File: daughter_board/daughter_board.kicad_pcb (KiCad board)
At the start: 2 copper layers, 54.1 x 62.5 mm, 30 parts, among them J1 Conn_01x05_Female, J3 Conn_01x06_Male, J4 Conn_01x06_Male, J5 Conn_01x02_Male, J6 Conn_01x02_Male, J7 Conn_01x06_Male, J8 Conn_01x06_Male, U1 ATmega32U4-A, U2 DRV8833PW, U3 DRV8833PW, U4 DRV8833PW, Y1 Crystal

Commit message: im so tired
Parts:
- removed C10: 0.1uF, Capacitor_SMD:C_0805_2012Metric
- removed C12: 2.2uF, Capacitor_SMD:C_0805_2012Metric
- removed C13: 10uF, Capacitor_SMD:C_0805_2012Metric
- removed J5, J6: Conn_01x02_Male, Connector_PinHeader_1.27mm:PinHeader_1x02_P1.27mm_Vertical
- removed U3: DRV8833PW, Package_SO:TSSOP-16_4.4x5mm_P0.65mm
- added SW1: SW_Push, Button_Switch_SMD:SW_SPST_EVPBF, F.Cu at (76.3, 100.2)
- C1, C11, C14, C15, C2, C3, C4, C5, C6, C7, C8, C9: footprint Capacitor_SMD:C_0805_2012Metric -> Capacitor_SMD:C_0402_1005Metric
- Y1: footprint Crystal:Crystal_SMD_SeikoEpson_FA238-4Pin_3.2x2.5mm -> Crystal:TXC_A308000003
- moved J8 61.0 mm to (66.1, 104.3)
- moved C11 54.2 mm to (69.7, 99.1)
- moved J4 53.1 mm to (58.7, 104.1), turned to -90 degrees
- moved C3 49.7 mm to (51.7, 100.8), turned to 150 degrees
- moved C8 42.2 mm to (49.0, 92.8)
- moved C14 39.6 mm to (69.2, 97.6), turned to 90 degrees
- moved R2 39.1 mm to (48.7, 101.4)
- moved C9 38.0 mm to (46.9, 86.0)
- moved C6 37.7 mm to (49.7, 86.8), turned to -120 degrees
- moved R1 37.2 mm to (48.7, 100.2)
- moved C5 36.6 mm to (50.8, 87.5), turned to -120 degrees
- moved U4 36.6 mm to (65.7, 98.6), turned to 90 degrees
- moved C1 35.0 mm to (47.6, 92.5), turned to 150 degrees
- moved U2 34.8 mm to (46.0, 89.4), turned to 0 degrees
- moved J3 33.7 mm to (40.8, 94.0)
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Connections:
- C15 pad 1: Net-(C15-Pad1) -> MOTOR_SUPPLY
- C9 pad 1: Net-(C9-Pad1) -> MOTOR_SUPPLY
- J8 pad 3: /D_ENC_1 -> Net-(J8-Pad3)
- J8 pad 6: Net-(J8-Pad6) -> /D_ENC_1
- U1 pad 13: unconnected-(U1-Pad13) -> RST
- U1 pad 20: MOTOR_B2_IN -> MOTOR_B1_IN
- U1 pad 21: MOTOR_B1_IN -> MOTOR_B2_IN
- U1 pad 28: /C_ENC_1 -> /C_ENC_2
- U1 pad 29: /C_ENC_2 -> /C_ENC_1
- U1 pad 31: MOTOR_A2_IN -> MOTOR_A1_IN
- U1 pad 32: MOTOR_A1_IN -> MOTOR_A2_IN
- U2 pad 12: Net-(C9-Pad1) -> MOTOR_SUPPLY
- U4 pad 12: Net-(C15-Pad1) -> MOTOR_SUPPLY
- U4 pad 7: Net-(J8-Pad6) -> Net-(J8-Pad3)
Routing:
- net Net-(J7-Pad2): track 0.00 -> 36.4 mm, vias 0 -> 2
- net Net-(J7-Pad1): track 0.00 -> 35.9 mm, vias 0 -> 2
- net +3V3: track 0.00 -> 34.5 mm, vias 0 -> 4
- net /D_ENC_1: track 0.00 -> 30.7 mm, vias 0 -> 2
- net GND: track 0.00 -> 30.1 mm, vias 0 -> 5
- net RST: track 0.00 -> 28.3 mm, vias 0 -> 2
- net /B_ENC_2: track 0.00 -> 28.2 mm, vias 0 -> 2
- net Net-(J4-Pad1): track 0.00 -> 24.5 mm
- net /B_ENC_1: track 0.00 -> 24.2 mm, vias 0 -> 2
- net Net-(J4-Pad2): track 0.00 -> 22.6 mm
- net /C_ENC_2: track 0.00 -> 18.8 mm
- net /C_ENC_1: track 0.00 -> 16.1 mm
- net MOTOR_A2_IN: track 0.00 -> 15.3 mm, vias 0 -> 1
- net MOTOR_B2_IN: track 0.00 -> 14.1 mm, vias 0 -> 1
- net MOTOR_C1_IN: track 0.00 -> 14.0 mm, vias 0 -> 1
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- added copper zone on In1.Cu, net +3V3
- added copper zone on B.Cu, net GND
- added copper zone on F.Cu, net GND
- added copper zone on In1.Cu, net GND
- added copper zone on In2.Cu, net GND
- added copper zone on In2.Cu, net MOTOR_SUPPLY
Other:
- board size 54.1 x 62.5 mm -> 54.1 x 31.2 mm
- copper layers 2 -> 4
- board text added: "3V3"
- board text added: "ENC"
- board text added: "GND"
- board text added: "M_Out"
- board text added: "RST"
- board text added: "SCL"
- board text added: "SDA"
- board text added: "VM"

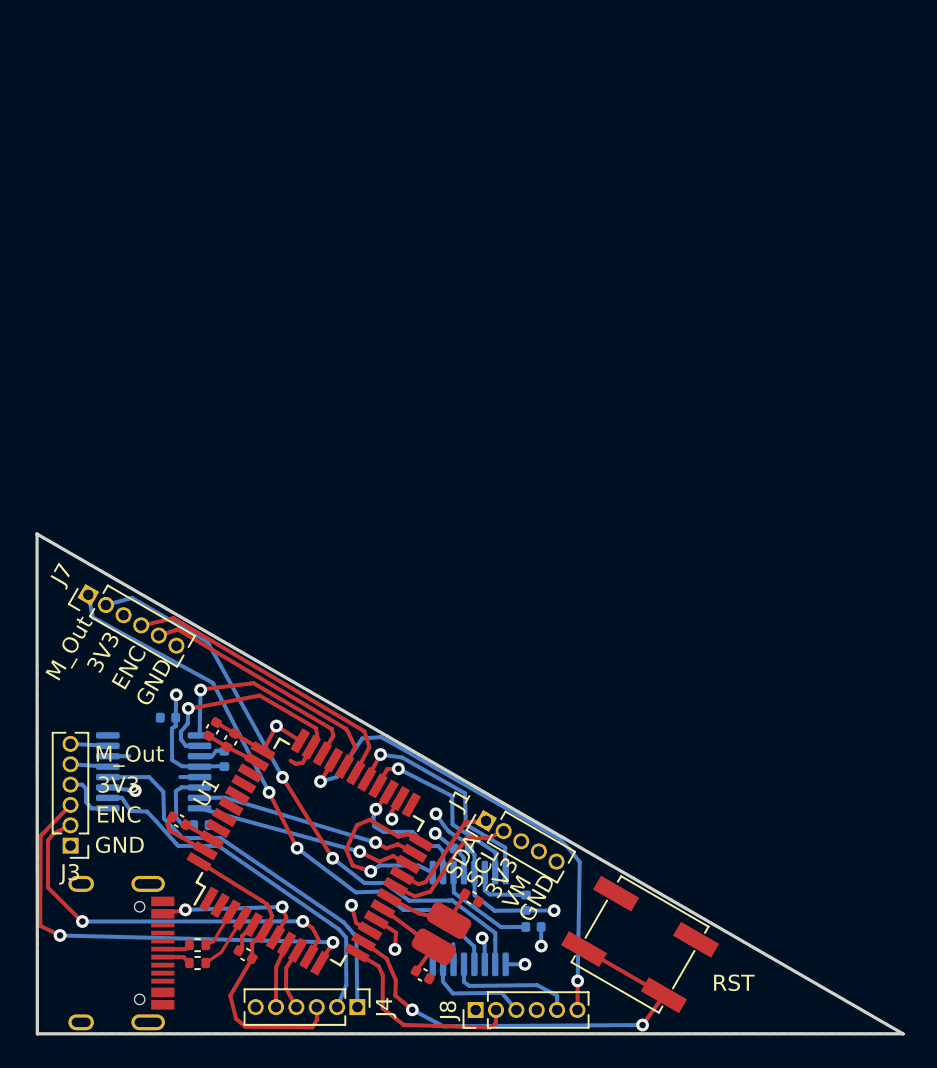
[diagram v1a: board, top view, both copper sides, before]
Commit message: Added daughter board
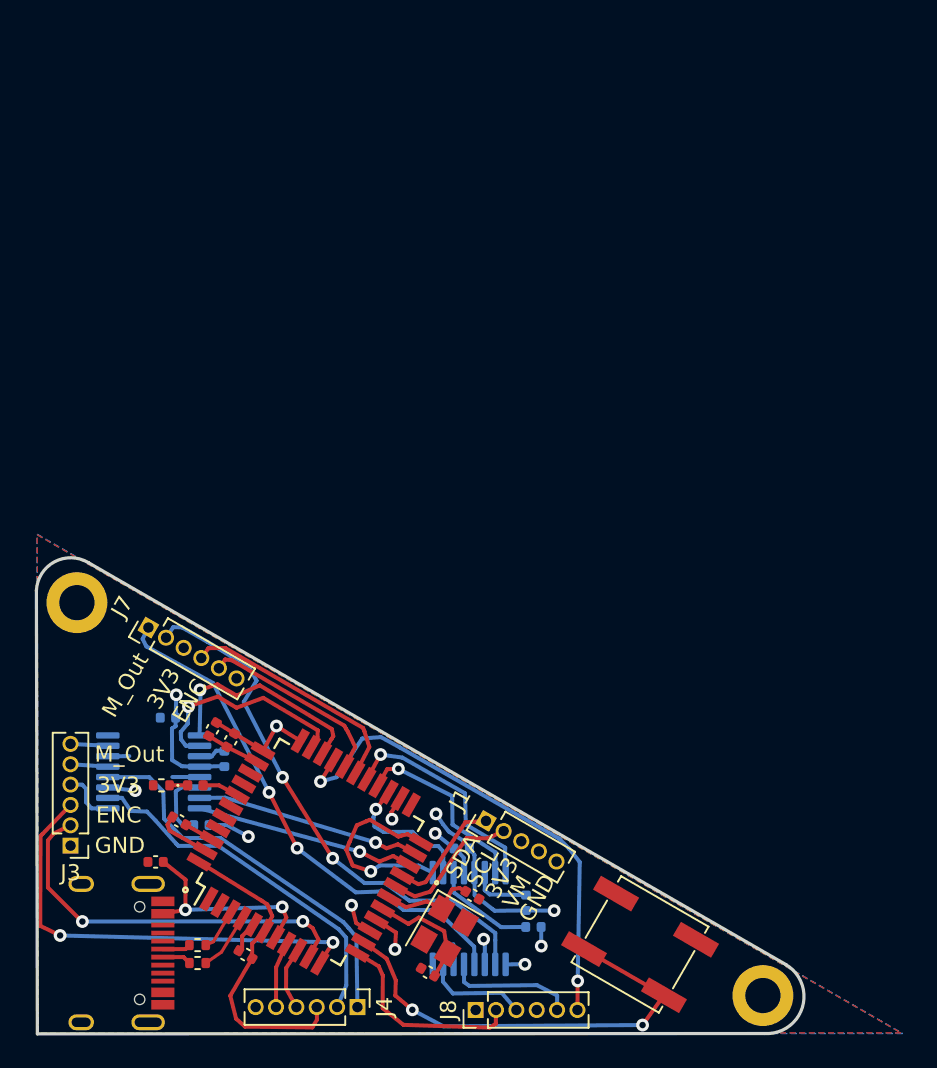
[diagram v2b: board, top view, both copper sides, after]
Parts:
- added C10: 0.1uF, Capacitor_SMD:C_0402_1005Metric, F.Cu at (46.1, 95.0)
- added D1: LED, LED_SMD:LED_0402_1005Metric, F.Cu at (48.6, 90.3)
- added H1: MountingHole_Pad, MountingHole:MountingHole_2.2mm_M2_DIN965_Pad, F.Cu at (84.0, 103.4)
- added H2: MountingHole_Pad, MountingHole:MountingHole_2.2mm_M2_DIN965_Pad, F.Cu at (41.2, 78.9)
- added R3: 220, Resistor_SMD:R_0402_1005Metric, F.Cu at (46.5, 90.3)
- C2, C4: value 15pF -> 12pF
- Y1: value Crystal -> Crystal_GND24; footprint Crystal:TXC_A308000003 -> Crystal:Crystal_SMD_3225-4Pin_3.2x2.5mm
- moved J7 4.27 mm to (45.7, 80.4)
- moved Y1 0.71 mm to (64.2, 99.4)
- moved C4 0.36 mm to (63.1, 101.9), turned to 150 degrees
- moved C2 0.16 mm to (65.9, 97.1)
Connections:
- U1 pad 38: MOTOR_E1_IN -> Net-(D1-Pad2)
- U1 pad 39: MOTOR_E2_IN -> unconnected-(U1-Pad39)
- U1 pad 40: MOTOR_F1_IN -> unconnected-(U1-Pad40)
- U1 pad 41: MOTOR_F2_IN -> unconnected-(U1-Pad41)
- Y1 pad 2: XTAL2 -> unconnected-(Y1-Pad2)
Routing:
- net /C_ENC_1: track 16.1 -> 12.1 mm
- net /C_ENC_2: track 18.8 -> 14.8 mm
- net Net-(J7-Pad1): track 35.9 -> 32.0 mm
- net VBUS: track 9.60 -> 13.3 mm
- net GND: track 30.1 -> 33.1 mm, vias 5 -> 6
- net +3V3: track 34.5 -> 37.6 mm
- net Net-(J7-Pad2): track 36.4 -> 33.6 mm
- net Net-(D1-Pad2): track 0.00 -> 2.29 mm
- net MOTOR_A2_IN: track 15.3 -> 13.8 mm
- net Net-(D1-Pad1): track 0.00 -> 1.12 mm
- net XTAL2: track 6.54 -> 7.46 mm
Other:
- board size 54.1 x 31.2 mm -> 47.9 x 29.7 mm
- board text removed: "RST"
